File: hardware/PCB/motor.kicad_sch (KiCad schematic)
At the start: 20 parts, among them M1 Turntable Stepper, M2 Gantry Stepper, M3 Extruder Stepper, M4 Revolute Stepper

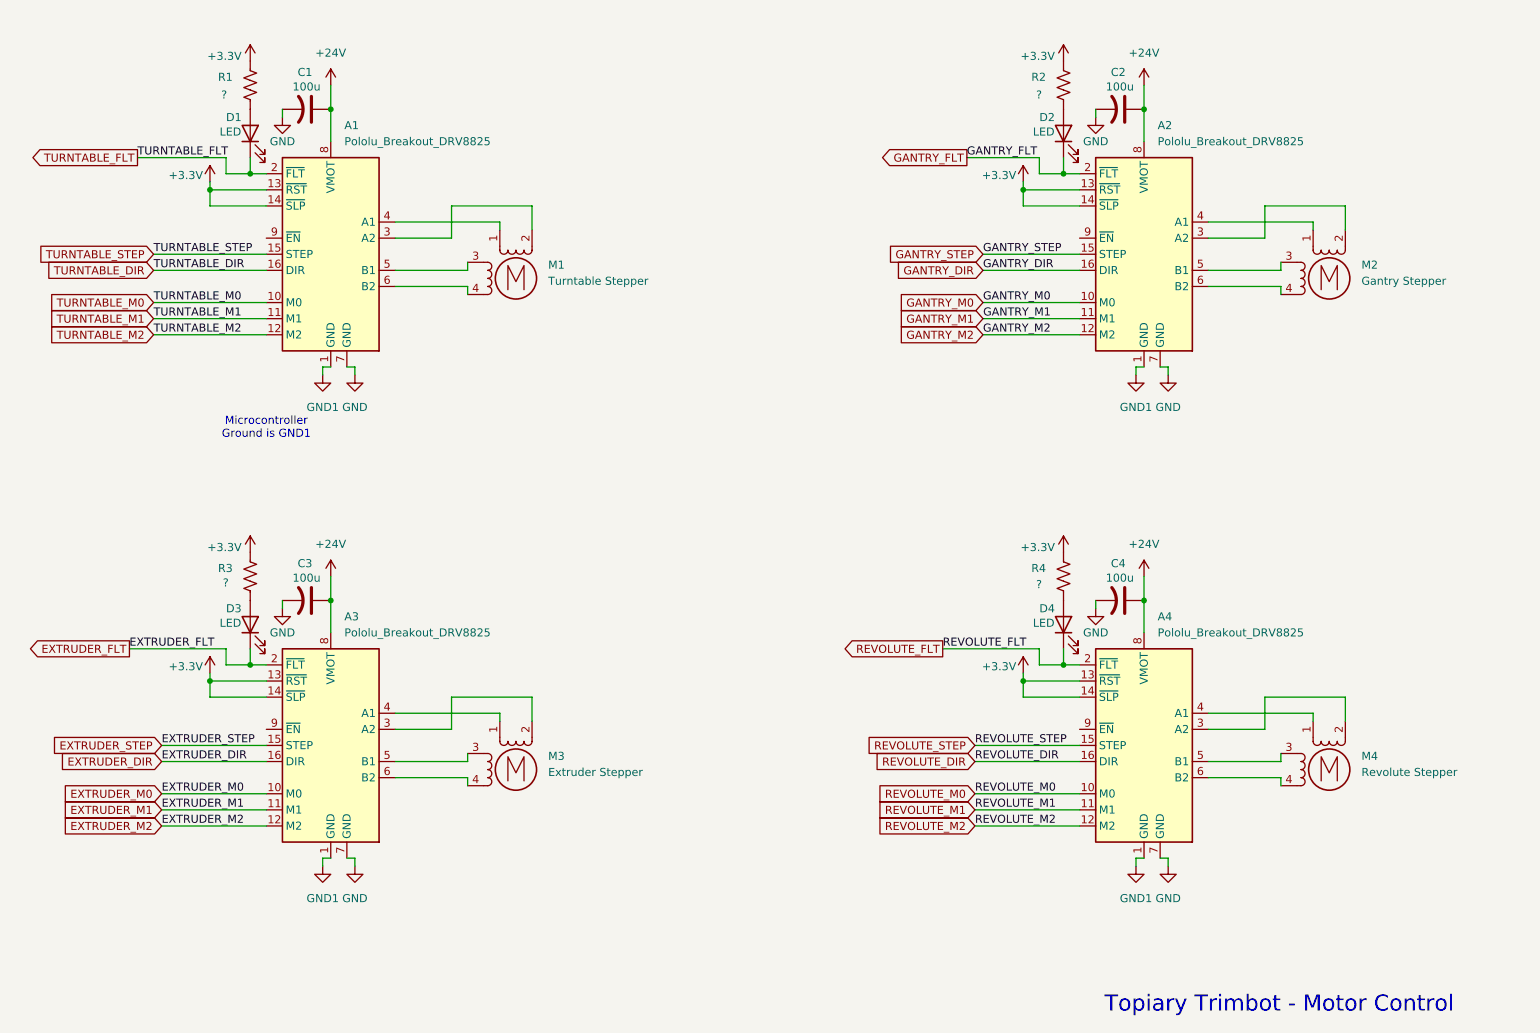
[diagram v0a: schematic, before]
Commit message: Schematic - Driver Enable Jumpers
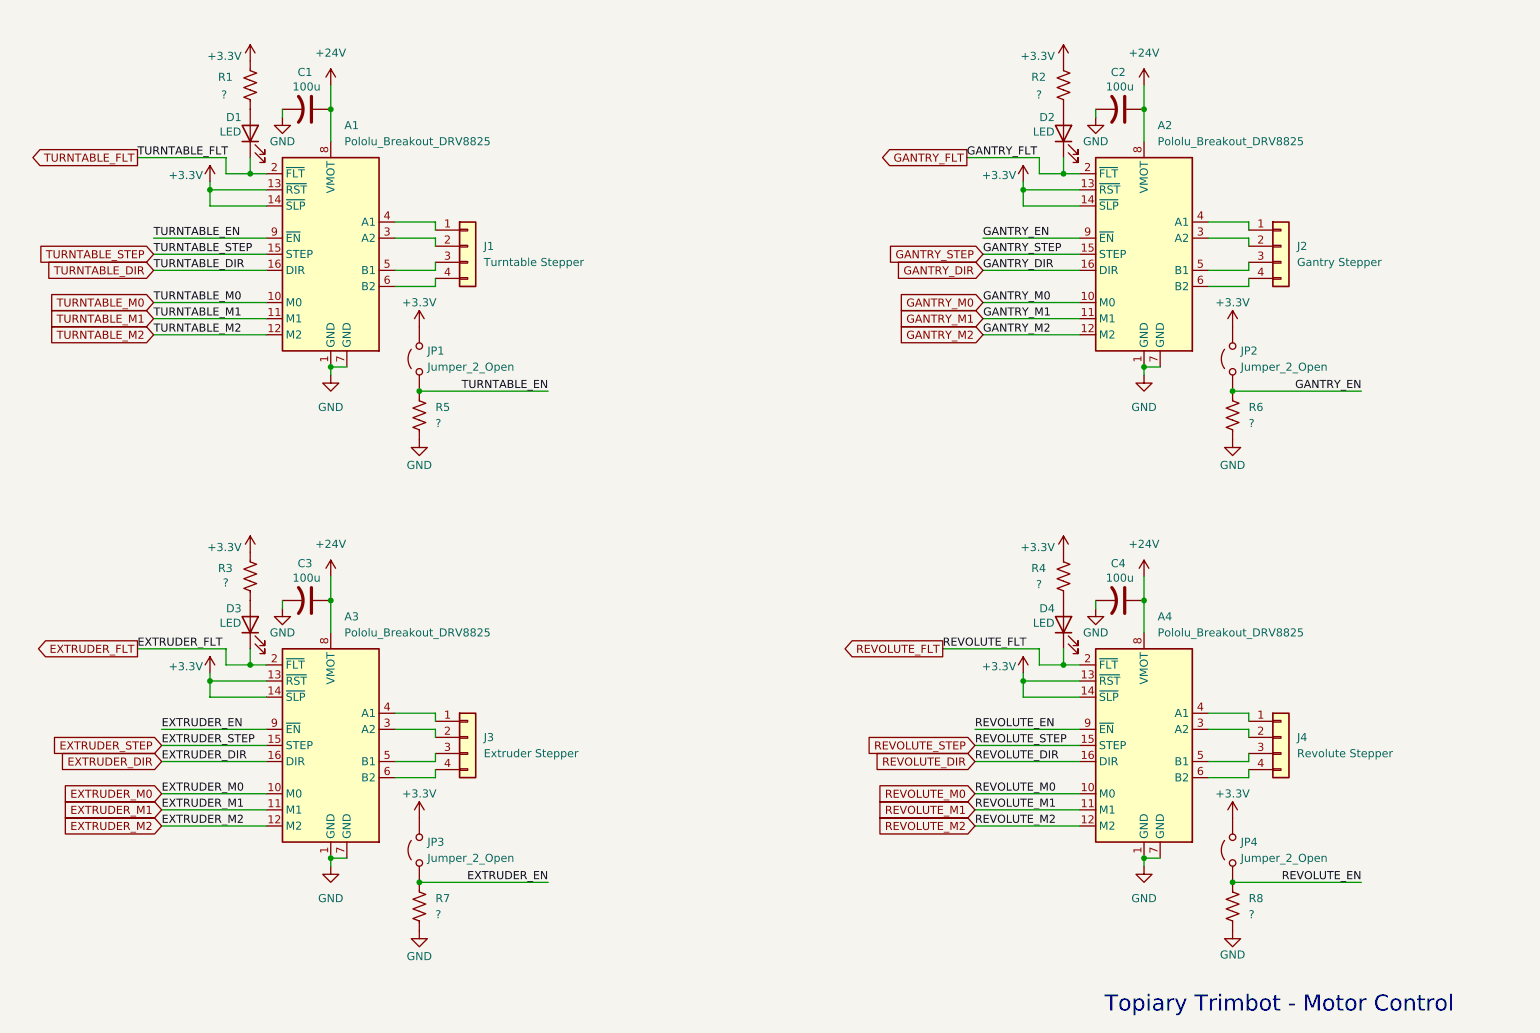
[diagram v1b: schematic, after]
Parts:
- removed M1: Turntable Stepper, symbol Motor:Stepper_Motor_bipolar
- removed M2: Gantry Stepper, symbol Motor:Stepper_Motor_bipolar
- removed M3: Extruder Stepper, symbol Motor:Stepper_Motor_bipolar
- removed M4: Revolute Stepper, symbol Motor:Stepper_Motor_bipolar
- added J1: Turntable Stepper, symbol Connector_Generic:Conn_01x04
- added J2: Gantry Stepper, symbol Connector_Generic:Conn_01x04
- added J3: Extruder Stepper, symbol Connector_Generic:Conn_01x04
- added J4: Revolute Stepper, symbol Connector_Generic:Conn_01x04
- added JP1, JP2, JP3, JP4: Jumper_2_Open, symbol Jumper:Jumper_2_Open
- added R5, R6, R7, R8: ?, symbol Device:R_US
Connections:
- net GND1 is gone; now on net GND: A1.1 (GND), A2.1 (GND), A3.1 (GND), A4.1 (GND)
- net +3.3V: now also JP1.2 (B), JP2.2 (B), JP3.2 (B), JP4.2 (B)
- net GND: now also R5.2, R6.2, R7.2, R8.2
- net at A4.3 (A2): now also J4.2 (Pin_2)
- net at A4.4 (A1): now also J4.1 (Pin_1)
- net at A4.5 (B1): now also J4.3 (Pin_3)
- net at A4.6 (B2): now also J4.4 (Pin_4)
- net REVOLUTE_EN: now reaches A4.9 (~{EN})
- net REVOLUTE_EN: now also JP4.1 (A), R8.1
- net at A2.4 (A1): now also J2.1 (Pin_1)
- net at A2.3 (A2): now also J2.2 (Pin_2)
- net at A2.5 (B1): now also J2.3 (Pin_3)
- net at A2.6 (B2): now also J2.4 (Pin_4)
- net at A3.3 (A2): now also J3.2 (Pin_2)
- net at A3.4 (A1): now also J3.1 (Pin_1)
- net at A3.5 (B1): now also J3.3 (Pin_3)
- net at A3.6 (B2): now also J3.4 (Pin_4)
- net EXTRUDER_EN: now reaches A3.9 (~{EN})
- net EXTRUDER_EN: now also JP3.1 (A), R7.1
- net GANTRY_EN: now reaches A2.9 (~{EN})
- net GANTRY_EN: now also JP2.1 (A), R6.1
- net at A1.3 (A2): now also J1.2 (Pin_2)
- net at A1.4 (A1): now also J1.1 (Pin_1)
- net at A1.5 (B1): now also J1.3 (Pin_3)
- net at A1.6 (B2): now also J1.4 (Pin_4)
- net TURNTABLE_EN: now reaches A1.9 (~{EN})
- net TURNTABLE_EN: now also JP1.1 (A), R5.1
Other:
- note removed: "Microcontroller Ground is GND1"

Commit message: Schematic - Driver VDD Jumpers
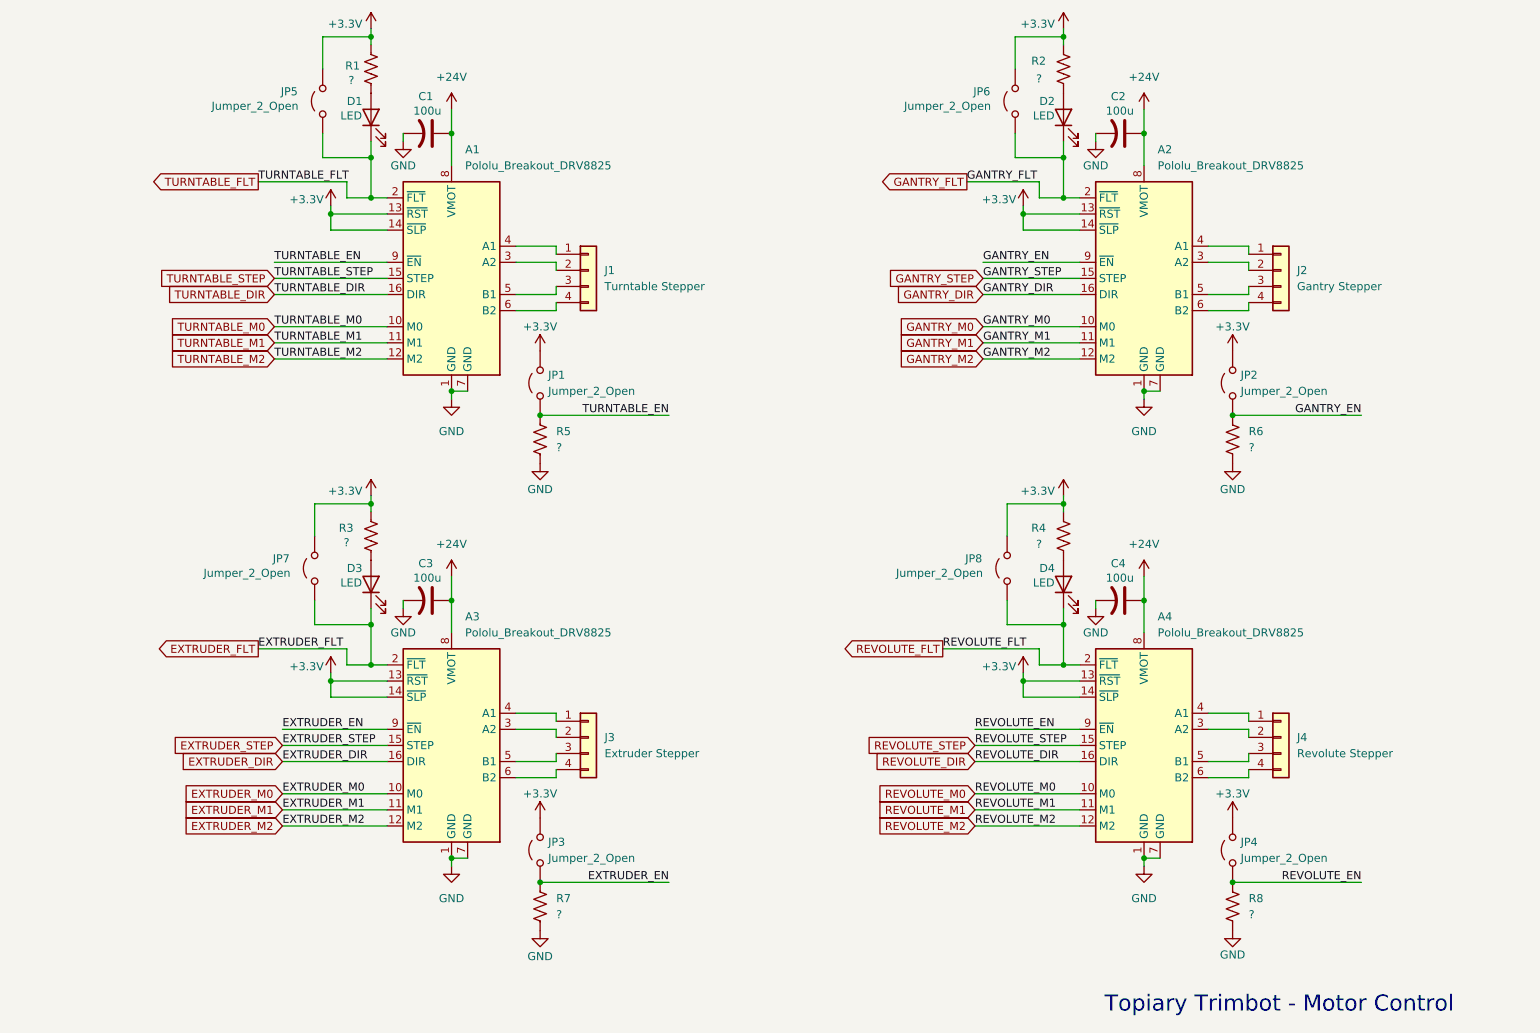
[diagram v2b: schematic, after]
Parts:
- added JP5, JP6, JP7, JP8: Jumper_2_Open, symbol Jumper:Jumper_2_Open
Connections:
- net +3.3V: now also JP5.2 (B), JP6.2 (B), JP7.2 (B), JP8.2 (B)
- net EXTRUDER_FLT: now also JP7.1 (A)
- net GANTRY_FLT: now also JP6.1 (A)
- net REVOLUTE_FLT: now also JP8.1 (A)
- net TURNTABLE_FLT: now also JP5.1 (A)
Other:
- moved on the sheet: A1, A2, A3, C1, C2, C3, D1, D2, D3, D4, J1, J2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
